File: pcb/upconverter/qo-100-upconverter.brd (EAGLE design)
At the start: 90 x 57 mm, 172 parts, among them CON1 3P-SH-SIDE, CON2 2EDG-2P-5MM, U1 EFM32TG11B120F128GM32, U10 MIC23155, U11 LT8636, U12 MCP3421-A0, U13 MCP6C02-020, U14 ADP7142AUJZ-3.3, U15 ADP7142AUJZ-3.3, U16 ADP3334, U17 ADM7171ACPZ-5.0, U2 DSB321SDA, U3 ADF4351, U4 F1951NBGI, U5 MAX2671, U6 2450BP15E0100, U7 F1478NLGA, U8 F1951NBGI, U9 ADL5606

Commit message: Upconverter assembly BOM changes
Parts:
- C25: value 100nF -> 150pF
- C27: value 100nF -> 150pF + 18 nH
- R4, R5: value 0 Ohms -> 100 Ohms
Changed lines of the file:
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@@
 <drawing>
 <settings>
-<setting alwaysvectorfont="yes"/>
+<setting alwaysvectorfont="no"/>
 <setting verticaltext="up"/>
 </settings>
@@
 </autorouter>
 <elements>
-<element name="C25" library="Capacitor" package="CAP0603" value="100nF" x="81.5" y="45.25" smashed="yes" rot="R180">
+<element name="C25" library="Capacitor" package="CAP0603" value="150pF" x="81.5" y="45.25" smashed="yes" rot="R180">
 <attribute name="NAME" x="81.2536" y="46.666" size="0.8" layer="25" font="vector" ratio="10" rot="SR0" align="center-left"/>
 <attribute name="VALUE" x="84.4464" y="47.282" size="0.8" layer="27" font="vector" ratio="10" rot="SR180" align="center-left"/>
@@
 <attribute name="VALUE" x="72.38" y="45.655" size="0.8" layer="27" font="vector" ratio="10" align="center-left"/>
 </element>
-<element name="C27" library="Capacitor" package="CAP0603" value="100nF" x="69.5" y="44" smashed="yes" rot="R180">
+<element name="C27" library="Capacitor" package="CAP0603" value="150pF + 18 nH" x="69.5" y="44" smashed="yes" rot="R180">
 <attribute name="NAME" x="67.9536" y="45.416" size="0.8" layer="25" font="vector" ratio="10" rot="SR0" align="center-left"/>
 <attribute name="VALUE" x="72.4464" y="46.032" size="0.8" layer="27" font="vector" ratio="10" rot="SR180" align="center-left"/>
@@
 <attribute name="VALUE" x="89.905" y="30.58" size="0.8" layer="27" font="vector" ratio="10" rot="R180" align="center-left"/>
 </element>
-<element name="R4" library="Resistor" package="RES0603" value="0 Ohms" x="81.5" y="24.1" smashed="yes" rot="R180">
+<element name="R4" library="Resistor" package="RES0603" value="100 Ohms" x="81.5" y="24.1" smashed="yes" rot="R180">
 <attribute name="NAME" x="78.4456" y="24.116" size="0.8" layer="25" font="vector" ratio="10" rot="SR0" align="center-left"/>
 <attribute name="TOLERANCE" value="" x="81.5" y="20.8" size="0.8" layer="27" font="vector" ratio="10" rot="R180" display="off"/>
 <attribute name="VALUE" x="84.9544" y="26.132" size="0.8" layer="27" font="vector" ratio="10" rot="SR180" align="center-left"/>
 </element>
-<element name="R5" library="Resistor" package="RES0603" value="0 Ohms" x="81.5" y="25.9" smashed="yes" rot="R180">
+<element name="R5" library="Resistor" package="RES0603" value="100 Ohms" x="81.5" y="25.9" smashed="yes" rot="R180">
 <attribute name="NAME" x="78.4456" y="25.916" size="0.8" layer="25" font="vector" ratio="10" rot="SR0" align="center-left"/>
 <attribute name="TOLERANCE" value="" x="81.5" y="22.6" size="0.8" layer="27" font="vector" ratio="10" rot="R180" display="off"/>

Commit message: Tweaking upconverter performance
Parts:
- C22: value 68nF -> 1uF
- C23: value 2.7nF -> 220nF
- C24: value 910pF -> 2.7nF
- R13: value 866 Ohms -> 150 Ohms
- R15: value 6.65K Ohms -> 1K Ohms
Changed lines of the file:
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@@
 <attribute name="VOLTAGE" value="" x="22.16" y="120.13" size="1.778" layer="27" rot="R180" display="off"/>
 </element>
-<element name="C22" library="Capacitor" package="CAP0603" value="68nF" x="71.7" y="27.3" smashed="yes">
+<element name="C22" library="Capacitor" package="CAP0603" value="1uF" x="71.7" y="27.3" smashed="yes">
 <attribute name="NAME" x="68.0536" y="27.416" size="0.8" layer="25" font="vector" ratio="10" rot="SR0" align="center-left"/>
 <attribute name="VALUE" x="68.7536" y="25.268" size="0.8" layer="27" font="vector" ratio="10" rot="SR0" align="center-left"/>
 <attribute name="VOLTAGE" value="" x="117.42" y="-60.33" size="1.778" layer="27" display="off"/>
 </element>
-<element name="C23" library="Capacitor" package="CAP0603" value="2.7nF" x="71.7" y="30.7" smashed="yes">
+<element name="C23" library="Capacitor" package="CAP0603" value="220nF" x="71.7" y="30.7" smashed="yes">
 <attribute name="NAME" x="71.4536" y="32.116" size="0.8" layer="25" font="vector" ratio="10" rot="SR0" align="center-left"/>
 <attribute name="VALUE" x="68.7536" y="28.668" size="0.8" layer="27" font="vector" ratio="10" rot="SR0" align="center-left"/>
 <attribute name="VOLTAGE" value="" x="122.5" y="-56.93" size="1.778" layer="27" display="off"/>
 </element>
-<element name="C24" library="Capacitor" package="CAP0603" value="910pF" x="74.4" y="29.9" smashed="yes" rot="R90">
+<element name="C24" library="Capacitor" package="CAP0603" value="2.7nF" x="74.4" y="29.9" smashed="yes" rot="R90">
 <attribute name="NAME" x="75.784" y="28.3536" size="0.8" layer="25" font="vector" ratio="10" rot="SR90" align="center-left"/>
 <attribute name="VALUE" x="76.432" y="26.9536" size="0.8" layer="27" font="vector" ratio="10" rot="SR90" align="center-left"/>
@@
 <attribute name="VALUE" x="75.1544" y="27.632" size="0.8" layer="27" font="vector" ratio="10" rot="SR180" align="center-left"/>
 </element>
-<element name="R13" library="Resistor" package="RES0603" value="866 Ohms" x="74.4" y="26.5" smashed="yes" rot="R90">
+<element name="R13" library="Resistor" package="RES0603" value="150 Ohms" x="74.4" y="26.5" smashed="yes" rot="R90">
 <attribute name="NAME" x="75.884" y="25.0456" size="0.8" layer="25" font="vector" ratio="10" rot="SR90" align="center-left"/>
 <attribute name="TOLERANCE" value="" x="126.47" y="100.16" size="1.778" layer="27" rot="R90" display="off"/>
 <attribute name="VALUE" x="76.432" y="23.0456" size="0.8" layer="27" font="vector" ratio="10" rot="SR90" align="center-left"/>
 </element>
-<element name="R15" library="Resistor" package="RES0603" value="6.65K Ohms" x="71.7" y="29" smashed="yes" rot="R180">
+<element name="R15" library="Resistor" package="RES0603" value="1K Ohms" x="71.7" y="29" smashed="yes" rot="R180">
 <attribute name="NAME" x="68.0456" y="28.416" size="0.8" layer="25" font="vector" ratio="10" rot="SR0" align="center-left"/>
 <attribute name="TOLERANCE" value="" x="-9.58" y="81.07" size="1.778" layer="27" rot="R180" display="off"/>

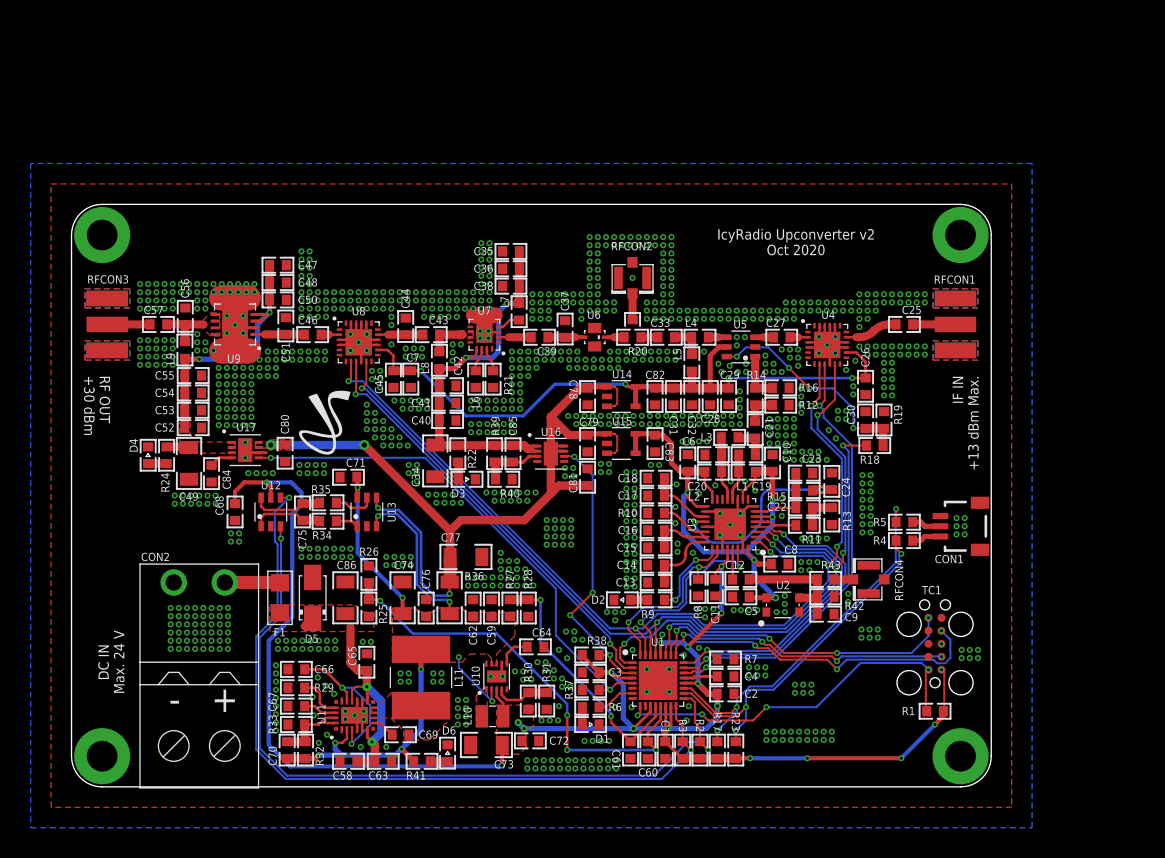
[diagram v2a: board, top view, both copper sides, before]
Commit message: Upconverter v3 sent to production
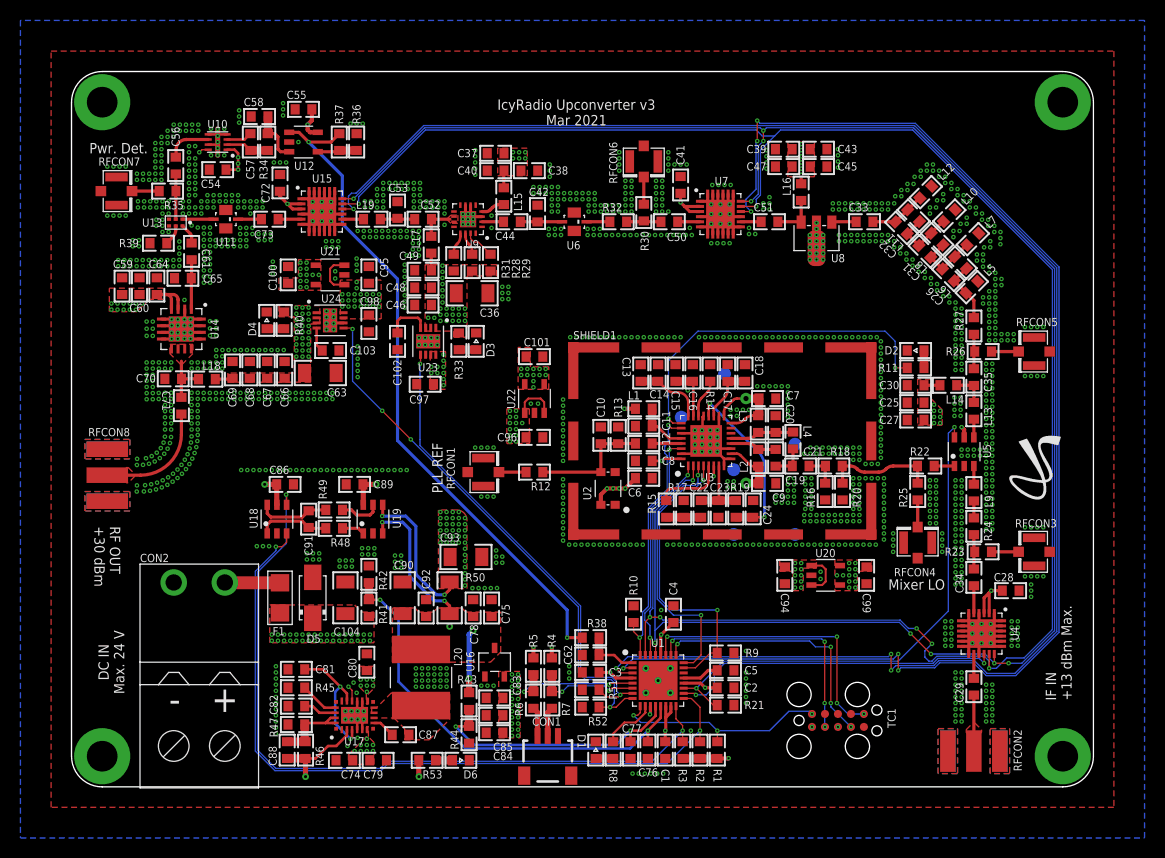
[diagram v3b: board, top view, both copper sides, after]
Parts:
- added C100, C101, C99: 10uF, Capacitor:CAP0603
- added C102, C103: 1nF, Capacitor:CAP0603
- added C104: 10uF, Capacitor:CAP1206
- added C87, C91, C92: 100nF, Capacitor:CAP0603
- added C88: 10pF, Capacitor:CAP0603
- added C89, C94, C95, C96, C97, C98: 1uF, Capacitor:CAP0603
- added C90: 100uF, Capacitor:CAP1206
- added C93: 22uF, Capacitor:CAP1206
- added L12, L13: 3.3nH, Inductor:IND0603
- added L14: 1.8nH, Inductor:IND0603
- added L15: 1.5nH, Inductor:IND0603
- added L16: 470nH, Inductor:IND0603
- added L17: 2.2nH, Inductor:IND0603
- added L18: 62nH, Inductor:IND0603
- added L19: 0 Ohms, Inductor:IND0603
- added L20: 4.7uH, Inductor:IND0606
- added R44: 75K Ohms, Resistor:RES0603
- added R45: 41.2K Ohms, Resistor:RES0603
- added R46: 1M Ohms, Resistor:RES0603
- added R47: 221K Ohms, Resistor:RES0603
- added R48, R49: 10K Ohms, Resistor:RES0603
- added R50: 0.03 Ohms, Resistor:RES1206
- added R51, R52: 100K Ohms, Resistor:RES0603
- added R53: 1K Ohms, Resistor:RES0603
- added RFCON5, RFCON6, RFCON7: RFCON-U.FL, RF Connector:U.FL
- added RFCON8: RFCON-SMA-EDGE, RF Connector:SMA-EDGE
- added SHIELD1: SHIELD-TE-2118728, Shield:2118728
- added TP1, TP2, TP3, TP4, TP5, TP6: TESTPOINT-1.27MM, PADs:PAD1.27MM
- added U18: MCP3421-A0, Microchip:SOT23-6
- added U19: MCP6C02-020, Microchip:SOT23-6
- added U20, U21, U22: ADP7142AUJZ-3.3, Analog Devices:SOT23-5
- added U23, U24: ADM7171ACPZ-5.0, Analog Devices:LFCSP8_3X3
- C10: value 100nF -> 10pF
- C25: value 150pF -> 1uF
- C26: value 100nF -> 1.2pF
- C27: value 150pF + 18 nH -> 100nF
- C28, C4: value 1uF -> 100nF
- C29: value 100nF -> 150pF
- C30: value 100pF -> 47pF
- C31: value 47pF -> 1.8pF
- C32: value 47pF -> 1.5pF
- C33: value 220pF -> 1.5pF
- C34: value 100uF -> 150pF; device Capacitor:CAP1206 -> Capacitor:CAP0603
- C35: value 1uF -> 220pF
- C36: value 1nF -> 100uF; device Capacitor:CAP0603 -> Capacitor:CAP1206
- C37: value 0.5pF -> 1uF
- C38, C55, C7: value 15pF -> 100nF
- C39: value 10pF -> 1uF
- C40: value 1uF -> 33pF
- C41: value 1nF -> 100nF
- C42: value 15pF -> 0.8pF
- C43, C9: value 10pF -> 100nF
- C44: value 1.2pF -> 10pF
- C45: value 100nF -> 47pF
- C46: value 15pF -> 1uF
- C47: value 10uF -> 15pF
- C48: value 10nF -> 100nF
- C49: value 100uF -> 33pF; device Capacitor:CAP1206 -> Capacitor:CAP0603
- C5: value 100nF -> 1uF
- C50: value 100pF -> 15pF
- C51: value 2pF -> 15pF
- C52: value 1uF -> 22pF
- C53: value 10nF -> 0.7pF
- C54: value 100pF -> 4.7uF
- C56: value 3.3pF -> 15pF
- C57: value 15pF -> 10nF
- C58: value 4.7uF -> 1uF
- C59: value 100nF -> 10uF
- C60: value 470pF -> 10nF
- C61: value 470pF -> 15pF
- C62: value 4.7uF -> 10nF
- C63: value 1uF -> 100uF; device Capacitor:CAP0603 -> Capacitor:CAP1206
- C64: value 470pF -> 100pF
- C65: value 1uF -> 2pF
- C68: value 100nF -> 100pF
- C69: value 100nF -> 15pF
- C70: value 10pF -> 3.3pF
- C71: value 1uF -> 15pF
- C73: value 100uF -> 15pF; device Capacitor:CAP1206 -> Capacitor:CAP0603
- C74: value 100uF -> 4.7uF; device Capacitor:CAP1206 -> Capacitor:CAP0603
- C76: value 100nF -> 470pF
- C77: value 22uF -> 470pF; device Capacitor:CAP1206 -> Capacitor:CAP0603
- C78: value 1uF -> 4.7uF
- C82: value 10uF -> 10nF
- C83: value 10uF -> 100nF
- C84: value 1nF -> 10uF
- C85: value 470pF -> 10uF
- C86: value 10uF -> 100nF; device Capacitor:CAP1206 -> Capacitor:CAP0603
- L1: value 3.3nH -> 1uH
- L10: value 2.2uH -> 3.9nH; device Inductor:IND2520 -> Inductor:IND0603
- L11: value 4.7uH -> 5.6nH; device Inductor:IND0606 -> Inductor:IND0603
- L2: value 10nH -> 3.3nH
- L3: value 3.3nH -> 10nH
- L5: value 1.8nH -> 4.7nH
- L6: value 3.9nH -> 12nH
- L7: value 3nH -> 3.3nH
- L8: value 62nH -> 3.9nH
- L9: value 62nH -> 18nH
- R10: value 5.1K Ohms -> 100K Ohms
- R11: value DNP -> 330 Ohms
- R12: value 105 Ohms -> 0 Ohms
- R13: value 150 Ohms -> 10K Ohms
- R14: value 61.9 Ohms -> 5.1K Ohms
- R15, R23: value 1K Ohms -> DNP
- R17: value 1K Ohms -> 150 Ohms
- R18: value 100 Ohms -> 61.9 Ohms
- R19: value 100K Ohms -> 1K Ohms
- R20: value 0 Ohms -> 105 Ohms; device Resistor:RES0603-SEL -> Resistor:RES0603
- R22, R24: value 510 Ohms -> 0 Ohms
- R25: value 100K Ohms -> DNP
- R26, R35: value 10K Ohms -> DNP
- R27: value 100K Ohms -> 0 Ohms
- R28: value 75K Ohms -> 1K Ohms
- R29: value 41.2K Ohms -> 0 Ohms
- R30: value 309K Ohms -> DNP
- R31: value 71.5K Ohms -> 1.5K Ohms
- R32: value 1M Ohms -> 0 Ohms
- R33: value 221K Ohms -> 510 Ohms
- R34: value 10K Ohms -> 0 Ohms
- R36: value 0.03 Ohms -> 1K Ohms; device Resistor:RES1206 -> Resistor:RES0603
- R37: value 100K Ohms -> 2K Ohms
- R38, R7: value 100K Ohms -> 100 Ohms
- R39: value 210K Ohms -> 49.9 Ohms
- R4, R5: value 100 Ohms -> 1K Ohms
- R40: value 64.9K Ohms -> 510 Ohms
- R41: value 510 Ohms -> 100K Ohms
- R43: value 0 Ohms -> 100K Ohms
- R6: value 330 Ohms -> 100 Ohms
- R8: value 100K Ohms -> 330 Ohms
- R9: value 330 Ohms -> 100K Ohms
- RFCON1, RFCON3: value RFCON-SMA-EDGE -> RFCON-U.FL; device RF Connector:SMA-EDGE -> RF Connector:U.FL
- RFCON2: value RFCON-U.FL -> RFCON-SMA-EDGE; device RF Connector:U.FL -> RF Connector:SMA-EDGE
- U10: value MIC23155 -> LTC5597; device Microchip:DFN10 -> Analog Devices:DFN8_2X2
- U11: value LT8636 -> 2450BP15E0100; device Analog Devices:QFN20_ASYM_CORNER -> Generic Filter:2450BP15E0100
- U12: value MCP3421-A0 -> MCP6V31; device Microchip:SOT23-6 -> Microchip:SOT23-5
- U13: value MCP6C02-020 -> DC2337J5010AHF; device Microchip:SOT23-6 -> Anaren:DC2337J5010AHF
- U14: value ADP7142AUJZ-3.3 -> ADL5606; device Analog Devices:SOT23-5 -> Analog Devices:LFCSP16_4X4
- U15: value ADP7142AUJZ-3.3 -> F1958NBGK; device Analog Devices:SOT23-5 -> Renesas:QFN24_2
- U16: value ADP3334 -> MCP1700-330; device Analog Devices:LFCSP8_3X3 -> Microchip:SOT23
- U17: value ADM7171ACPZ-5.0 -> LT8636; device Analog Devices:LFCSP8_3X3 -> Analog Devices:QFN20_ASYM_CORNER
- U4: value F1951NBGI -> F1958NBGK; device Renesas:QFN24 -> Renesas:QFN24_2
- U7: value F1478NLGA -> F1958NBGK; device Renesas:QFN16 -> Renesas:QFN24_2
- U8: value F1951NBGI -> ADL5601; device Renesas:QFN24 -> Analog Devices:SOT89
- U9: value ADL5606 -> F1490NLGA; device Analog Devices:LFCSP16_4X4 -> Renesas:QFN16
- moved RFCON3 93.4 mm to (94.2, 23.0), turned to 180 degrees
- moved R24 79.3 mm to (88.3, 25.5), turned to 270 degrees
- moved L9 78.5 mm to (88.3, 28.8), turned to 90 degrees
- moved LOGO1 69.6 mm to (97.0, 34.5)
- moved C60 67.4 mm to (6.65, 49.0), turned to 90 degrees
- moved L10 66.3 mm to (85.9, 55.9), turned to 225 degrees
- moved L11 66.1 mm to (82.4, 55.9), turned to 135 degrees
- moved C61 65.0 mm to (11.8, 52.4)
- moved R26 63.9 mm to (89.2, 42.6), turned to 0 degrees
- moved C58 63.7 mm to (18.4, 65.6)
- moved R32 60.1 mm to (53.5, 55.3), turned to 0 degrees
- moved C72 59.8 mm to (20.4, 59.1), turned to 90 degrees
- moved U10 59.0 mm to (14.3, 63.1), turned to 180 degrees
- moved R37 59.0 mm to (26.2, 63.1), turned to 270 degrees
- moved RFCON2 57.1 mm to (88.3, 3.50), turned to 0 degrees
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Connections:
- removed net !IF_ATT_CS: U1.22, U4.9
- removed net !PA_STG1_BIAS_EN: R38.1, U1.3, U16.6
- removed net !RF_ATT_CS: U1.2, U8.9
- removed net 3V3_ATT_MIXER_CLEAN: C26.1, C28.1, C29.1, C31.1, C32.1, C45.1, C7.1, C82.1, L5.2, U14.4, U14.5, U4.14, U5.5, U8.14
- removed net 3V3_FB: R30.1, R31.2, U10.4
- removed net 3V3_SOFTSTART: C64.1, U10.6
- removed net 3V3_SW: L10.1, U10.1
- removed net 5V0_PA_STG1_CLEAN: C34.1, C35.1, C36.1, C38.1, C40.1, C41.1, C42.1, C85.1, L7.2, L8.2, R22.2, R39.2, U16.1, U16.2, U7.13
- removed net 5V0_PA_STG2_CLEAN: C47.1, C48.1, C49.1, C50.1, C52.1, C53.1, C54.1, C55.1, L9.2, R24.2, U17.1, U17.2, U17.3, U9.3, U9.4
- removed net N$14: C43.1, L8.1, U7.10, U7.11
- removed net N$18: C57.2, RFCON3.SIG
- removed net N$26: C25.2, U4.17
- removed net N$27: C27.2, U5.3
- removed net N$31: C33.2, R20.2
- removed net N$9: C46.1, U8.2
- removed net PA_STG2_BIAS_EN: R37.2, U1.5, U17.5
- removed net RF_ACC_FILT: C37.1, C39.1, U6.2
- removed net RF_ACC_PRE: C43.2, C44.1, U8.17
- new net 3V3_IF_ATT_MIXER_CLEAN: C25.1, C27.1, C28.1, C30.1, C99.1, L14.2, U20.4, U20.5, U4.2, U4.3, U5.5
- new net 3V3_RF_ATT_PDET_CLEAN: C100.1, C41.1, C54.1, C55.1, C72.1, U10.1, U10.8, U12.5, U15.2, U15.3, U21.4, U21.5, U7.2, U7.3
- new net 5V0_PA_STG1_2_CLEAN: C36.1, C37.1, C38.1, C39.1, C40.1, C43.1, C45.1, C46.1, C47.1, C48.1, C49.1, L15.2, L16.2, L17.2, R28.2, R29.2, R31.2, R33.2, U23.1, U23.2, U23.3
- new net 5V0_PA_STG3_CLEAN: C59.1, C60.1, C63.1, C64.1, C66.1, C67.1, C68.1, C69.1, L18.2, R40.2, U14.3, U14.4, U24.1, U24.2, U24.3
- new net IF_ATT_ACC: L9.1, R24.1
- new net IF_ATT_ACC_PROBE: C34.2, R23.1, R24.2
- new net IF_ATT_DCC: C34.1, U4.5
- new net IF_ATT_LE: U1.18, U4.16
- new net IF_IN_ACC: C29.2, U4.14
- new net MIXER_IN_DCC: L9.2, U5.3
- new net MIXER_OUT_ACC_PROBE: C35.2, R26.1, R27.2
- new net MIXER_OUT_DCC: L13.1, U5.4
- new net N$24: R23.2, RFCON3.P$3
- new net N$33: C31.2, C32.1, L10.2, L11.1, L8.2
- new net N$34: C32.2, C33.1, L11.2, L12.2
- new net N$35: R30.2, RFCON6.P$3
- new net N$39: L19.2, U15.14
- new net N$42: R39.2, U13.5
- new net N$43: C56.1, U10.6
- new net N$44: C57.2, U10.3
- new net N$45: R22.2, U5.1
- new net N$47: R25.1, RFCON4.P$3
- new net N$48: R35.2, RFCON7.P$3
- new net PA_STG1_2_BIAS_EN: R51.2, U1.7, U23.5
- new net PA_STG3_BIAS_EN: R52.2, U1.8, U24.5
- new net RF_ATT1_LE: U1.2, U7.16
- new net RF_ATT2_LE: U1.3, U15.16
- new net RF_FINAL_ACC: C71.2, RFCON8.SIG
- new net RF_FINAL_DCC: C70.1, C71.1, L18.1, U14.10, U14.11, U14.12, U14.9
- new net RF_LOL_FLT_ACC: C33.2, U8.1
- new net RF_PRE1_ACC: C51.2, U7.14
- new net RF_PRE1_ATT_ACC: R32.1, U6.4
- new net RF_PRE1_ATT_ACC_PROBE: C50.2, R30.1, R32.2
- new net RF_PRE1_ATT_DCC: C50.1, U7.5
- new net RF_PRE1_ATT_FLT_ACC: C42.1, C44.1, U6.2
- new net RF_PRE1_DCC: C51.1, L16.1, U8.3
- new net RF_PRE2_ACC: C52.2, C53.1, L19.1
- new net RF_PRE2_ATT_ACC: C73.2, U11.4
- new net RF_PRE2_ATT_DCC: C73.1, U15.5
- new net RF_PRE2_ATT_FLT_ACC: U11.2, U13.1
- new net RF_PRE2_ATT_FLT_CPL_ACC: C56.2, R35.1, U13.2
- new net RF_PRE2_ATT_FLT_THRU_ACC: C61.1, U13.6
- new net RF_PRE2_DCC: C52.1, L17.1, U9.10, U9.11
- new net VPDET_AMP: R37.1, R38.2, U12.1
- new net VPDET_FLT: C58.1, R34.1, U12.3
- new net VPDET_RAW: C57.1, R34.2, U10.2
- new net VPDET_SENSE: C62.1, R38.1, U1.1
- net !MIXER_SHDN: now also R21.2, U1.19, U5.6; no longer R18.2, U1.23
- net !PLL_MUTE: now also R10.2; no longer R8.2
- net 3V3: now also C4.1, C83.1, C84.1, C85.1, C86.1, R4.2, R5.2, U16.2, U18.5; no longer C11.1, C68.1, C72.1, C73.1, L10.2, R17.2, R23.2, R30.2, R38.2, U10.3, U12.5, U3.28
- net 3V3_PLL_CLEAN: now also C101.1, C7.1, C9.1, L1.2, L2.1, L3.2, U22.4, U22.5; no longer C10.1, C5.1, C83.1, L1.1, L2.2, U15.4, U15.5
- net 5V0: now also C75.1, C78.1, C88.1, C89.1, C90.1, C92.1, L20.2, R43.2, R46.2, R50.2, R53.2, U16.3, U17.2, U19.3, U19.6; no longer C59.1, C62.1, C70.1, C71.1, C74.1, C76.1, L11.2, R27.2, R32.2, R36.2, R41.2, U10.2, U10.8, U10.9, U11.2, U13.3, U13.6
- net 5V0_BST: now also C87.2, U17.7; no longer C69.2, U11.7
- net 5V0_FB: now also C88.2, R46.1, R47.2, U17.19, U17.20; no longer C70.2, R32.1, R33.2, U11.19, U11.20
- net 5V0_INTVCC: now also C81.1, U17.15, U17.3; no longer C66.1, U11.15, U11.3
- net 5V0_ISENSE: now also C93.1, C94.1, C95.1, C96.1, C97.1, C98.1, R50.1, U19.4, U20.1, U20.3, U21.1, U21.3, U22.1, U22.3, U23.7, U23.8, U24.7, U24.8; no longer C77.1, C78.1, C79.1, C80.1, C81.1, R36.1, U13.4, U14.1, U14.3, U15.1, U15.3, U16.7, U16.8, U16.9, U17.7, U17.8
- net 5V0_ISENSE_VN: now also C91.2, R49.1, U18.6; no longer C75.2, R35.1, U12.6
- net 5V0_ISENSE_VP: now also C91.1, R48.1, U18.1; no longer C75.1, R34.1, U12.1
- net 5V0_RT: now also R45.2, U17.17; no longer R29.2, U11.17
- net 5V0_SS: now also C82.1, U17.18; no longer C67.1, U11.18
- net 5V0_SW: now also C87.1, L20.1, U17.10, U17.8, U17.9; no longer C69.1, L11.1, U11.10, U11.8, U11.9
- net 5V0_VSENSE: now also C77.1, R43.1, R44.2; no longer C61.1, R27.1, R28.2
- net GND: now also C100.2, C101.2, C102.2, C103.2, C104.2, C25.2, C27.2, C39.2, C43.2, C46.2, C69.2, C70.2, C75.2, C85.2, C89.2, C90.2, C92.2, C93.2, C94.2, C95.2, C96.2, C97.2, C98.2, C99.2, L10.1, L12.1, L5.1, L7.1, R14.1, R17.1, R20.1, R36.1, R39.1, R44.1, R45.1, R47.1, R49.2, R51.1, R52.1, R9.1, RFCON1.P$1, RFCON1.P$2, RFCON2.GND@0, RFCON2.GND@1, RFCON2.GND@2, RFCON2.GND@3, RFCON3.P$1, RFCON3.P$2, RFCON5.P$1, RFCON5.P$2, RFCON6.P$1, RFCON6.P$2, RFCON7.P$1, RFCON7.P$2, RFCON8.GND@0, RFCON8.GND@1, RFCON8.GND@2, RFCON8.GND@3, SHIELD1.1, SHIELD1.10, SHIELD1.11, SHIELD1.12, SHIELD1.13, SHIELD1.14, SHIELD1.15, SHIELD1.16, SHIELD1.2, SHIELD1.3, SHIELD1.4, SHIELD1.5, SHIELD1.6, SHIELD1.7, SHIELD1.8, SHIELD1.9, TP1.TP, TP2.TP, TP3.TP, TP4.TP, TP5.TP, TP6.TP, U10.4, U10.5, U10.9, U11.1, U11.3, U13.3, U13.4, U14.13, U14.14, U14.15, U14.16, U14.17, U14.5, U14.6, U14.7, U14.8, U15.1, U15.10, U15.11, U15.12, U15.13, U15.15, U15.19, U15.20, U15.21, U15.22, U15.23, U15.24, U15.25, U15.4, U15.6, U15.7, U15.8, U15.9, U16.1, U17.12, U17.13, U17.21, U17.4, U17.5, U17.M1, U17.M2, U17.M3, U17.M4, U18.2, U19.2, U19.5, U20.2, U21.2, U22.2, U23.6, U23.9, U24.6, U24.9, U4.11, U4.7, U4.8, U4.9, U7.10, U7.11, U7.13, U7.15, U7.19, U7.20, U7.21, U7.22, U7.23, U7.24, U7.25, U7.4, U8.2, U9.1, U9.12, U9.3, U9.9; no longer C26.2, C29.2, C31.2, C32.2, C34.2, C35.2, C44.2, C50.2, C51.2, C52.2, C56.2, C61.2, C71.2, C73.2, L6.1, R12.1, R19.1, R26.1, R28.1, R29.1, R31.1, R33.1, R35.2, R37.1, R40.1, R7.1, R8.1, RFCON1.GND@0, RFCON1.GND@1, RFCON1.GND@2, RFCON1.GND@3, RFCON2.P$1, RFCON2.P$2, RFCON3.GND@0, RFCON3.GND@1, RFCON3.GND@2, RFCON3.GND@3, U10.10, U10.11, U11.12, U11.13, U11.21, U11.4, U11.5, U11.M1, U11.M2, U11.M3, U11.M4, U13.2, U13.5, U15.2, U16.5, U17.6, U17.9, U4.16, U4.18, U4.3, U7.17, U7.3, U7.5, U8.1, U8.10, U8.12, U8.13, U8.15, U8.16, U8.18, U8.19, U8.20, U8.21, U8.22, U8.23, U8.24, U8.25, U8.3, U8.6, U9.13, U9.14, U9.15, U9.16, U9.2
- net I2C0_SCL: now also R4.1, R7.2, U1.6; no longer R17.1, R5.2, U1.19
- net I2C0_SDA: now also R5.1, R6.2, U1.5; no longer R23.1, R4.2, U1.18
- net I2C1_SCL: now also U18.3; no longer U12.3
- net I2C1_SDA: now also U18.4; no longer U12.4
- net IF_IN_DCC: now also C29.1, RFCON2.SIG; no longer C25.1, RFCON1.SIG
- net LED: now also R8.2, U1.10; no longer R6.2, U1.7
- net MIXER_LO: now also R18.1, R20.2, R22.1, R25.2; no longer R14.1, R16.2, U5.1
- net N$1: now also L4.2; no longer L3.1
- net N$10: now also R48.2, U19.1; no longer R34.2, U13.1
- net N$11: now also R7.1; no longer R5.1
- net N$12: now also L15.1, U9.4; no longer L7.1, U7.4
- net N$13: now also R11.1; no longer R9.1
- net N$149: now also R53.1; no longer R41.1
- net N$15: now also R28.1, U9.14; no longer R21.2, U7.15
- net N$16: now also R31.1, U9.13; no longer L6.2, U7.14
- net N$17: now also R6.1; no longer R4.1
- net N$2: now also C103.1, U24.4; no longer C84.1, U17.4
- net N$20: now also C102.1, U23.4; no longer C85.2, R39.1, R40.2, U16.3
- net N$21: now also R12.2, RFCON1.P$3; no longer R43.2, RFCON4.P$3
- net N$22: now also C5.1; no longer C4.1
- net N$23: now also R33.1; no longer R22.1
- net N$25: now also R8.1; no longer R6.1
- net N$28: now also R26.2, RFCON5.P$3; no longer C27.1, U4.2
- net N$29: now also R16.2, R18.2; no longer R12.2, R14.2
- net N$3: now also R40.1; no longer R24.1
- net N$30: now also C44.2, U9.2; no longer C39.2, U7.2
- net N$32: now also C26.2, C31.1, L6.2, L7.2, L8.1; no longer R20.COM, RFCON2.P$3
- net N$4: now also R29.1, U9.15; no longer C30.1, R18.1, R19.2, U5.6
- net N$5: now also C61.2, C65.1, U14.1; no longer C46.2, C51.1, U9.1
- net N$6: now also C35.1, L13.2, L14.1; no longer C33.1, L4.2, L5.1
- net N$67: now also L3.1, L4.1; no longer L2.1, L3.2
- net N$69: now also L2.2; no longer L1.2
- net N$7: now also R36.2, R37.2, U12.4; no longer L4.1, U5.4
- net N$8: now also C11.1, L1.1, U3.28; no longer C56.1, C57.1, L9.1, U9.10, U9.11, U9.12, U9.9
- net N$84: now also R15.1, R17.2; no longer R11.1, R13.2
- net N$88: now also R14.2; no longer R10.2
- net PLL_CP_VOUT: now also R19.2; no longer R15.2
- net PLL_EN: now also R9.2, U1.23; no longer R7.2, U1.24
- net PLL_FASTLOCK_SW: now also R15.2; no longer R11.2
- net PLL_LE: now also U1.24; no longer U1.1
- net PLL_LOCK: now also R11.2; no longer R9.2
- net PLL_REF_DCC: now also C10.1, R12.1, R13.2; no longer C9.1, R42.2, R43.1
- net PLL_VTUNE: now also R19.1; no longer R15.1
- net RF_ACC: now also C26.1, L5.2, L6.1, R27.1; no longer R20.1, U6.4
- net SPI_MOSI: now also U15.18, U4.18, U7.18; no longer U4.11, U8.11
- net SPI_SCK: now also U15.17, U4.17, U7.17; no longer U4.8, U8.8
- net VIN: now also C104.1, C74.1, C79.1, C80.1, R41.2, U17.11, U17.14, U17.6; no longer C58.1, C63.1, C65.1, C86.1, R25.2, U11.11, U11.14, U11.6
- net VIN_VSENSE: now also C76.1, R41.1, R42.2; no longer C60.1, R25.1, R26.2
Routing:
- net RF_ATT2_LE: track 0.00 -> 165.8 mm, vias 0 -> 4
- net RF_ATT1_LE: track 0.00 -> 130.1 mm, vias 0 -> 6
- net 3V3: track 167.3 -> 59.4 mm, vias 18 -> 32
- net SPI_SCK: track 96.5 -> 190.6 mm, vias 6 -> 8
- net SPI_MOSI: track 98.3 -> 186.2 mm, vias 6 -> 10
- net 3V3_ATT_MIXER_CLEAN: track 66.2 -> 0.00 mm, vias 4 -> 0
- net VPDET_AMP: track 0.00 -> 66.1 mm, vias 0 -> 2
- net GND: track 90.9 -> 152.2 mm, vias 1120 -> 1519
- net 5V0_ISENSE: track 87.5 -> 27.5 mm, vias 4 -> 94
- net PA_STG3_BIAS_EN: track 0.00 -> 53.8 mm, vias 0 -> 4
- net PA_STG2_BIAS_EN: track 50.0 -> 0.00 mm, vias 2 -> 0
- net PA_STG1_2_BIAS_EN: track 0.00 -> 46.6 mm, vias 0 -> 2
- net !IF_ATT_CS: track 43.1 -> 0.00 mm, vias 2 -> 0
- net !RF_ATT_CS: track 42.3 -> 0.00 mm, vias 2 -> 0
- net 5V0_PA_STG1_CLEAN: track 38.2 -> 0.00 mm, vias 2 -> 0
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- added copper zone on layer 15, net 3V3
- added copper zone on layer 1, net 3V3_IF_ATT_MIXER_CLEAN
- added copper zone on layer 15, net 3V3_IF_ATT_MIXER_CLEAN
- added copper zone on layer 1, net 3V3_PLL_CLEAN
- added copper zone on layer 15, net 3V3_PLL_CLEAN
- added copper zone on layer 1, net 3V3_RF_ATT_PDET_CLEAN
- added copper zone on layer 15, net 3V3_RF_ATT_PDET_CLEAN
- added copper zone on layer 15, net 5V0_ISENSE
- added copper zone on layer 1, net 5V0_PA_STG1_2_CLEAN
- added copper zone on layer 15, net 5V0_PA_STG1_2_CLEAN
- added copper zone on layer 1, net 5V0_PA_STG3_CLEAN
- added copper zone on layer 15, net 5V0_PA_STG3_CLEAN
- added copper zone on layer 15, net GND
- added copper zone on layer 2, net GND
- added copper zone on layer 1, net IF_IN_DCC
- added copper zone on layer 1, net RF_FINAL_ACC
- added copper zone on layer 1, net RF_FINAL_DCC
- added copper zone on layer 1, net RF_PRE2_DCC
- added copper zone on layer 15, net VIN
- removed copper zone on layer 1, net 3V3_SW
- removed copper zone on layer 1, net 5V0_PA_STG2_CLEAN
- removed copper zone on layer 1, net N$14
- removed copper zone on layer 1, net N$8
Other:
- board size 90 x 57 mm -> 100 x 70 mm
- board text added: "IcyRadio Upconverter v3 Mar 2021"
- board text added: "Mixer LO"
- board text added: "PLL REF"
- board text added: "Pwr. Det."
- board text removed: "IcyRadio Upconverter v2 Oct 2020"

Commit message: Update I2C slave resistors to minimize load effect when powered down
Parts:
- R4, R5: value 1K Ohms -> 47K Ohms
- R6, R7: value 100 Ohms -> 1K Ohms
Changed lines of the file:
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@@
 <attribute name="VALUE" x="51.68" y="0.095" size="0.8" layer="27" font="vector" ratio="10" rot="R90" align="center-left"/>
 </element>
-<element name="R6" library="Resistor" package="RES0603" value="100 Ohms" x="45.2" y="8.5" smashed="yes" rot="R90">
+<element name="R6" library="Resistor" package="RES0603" value="1K Ohms" x="45.2" y="8.5" smashed="yes" rot="R90">
 <attribute name="NAME" x="43.784" y="6.9456" size="0.8" layer="25" font="vector" ratio="10" rot="SR90" align="center-left"/>
 <attribute name="TOLERANCE" value="" x="41.9" y="8.5" size="0.8" layer="27" font="vector" ratio="10" rot="R90" display="off"/>
 <attribute name="VALUE" x="47.232" y="5.0456" size="0.8" layer="27" font="vector" ratio="10" rot="SR90" align="center-left"/>
 </element>
-<element name="R7" library="Resistor" package="RES0603" value="100 Ohms" x="47" y="8.5" smashed="yes" rot="R90">
+<element name="R7" library="Resistor" package="RES0603" value="1K Ohms" x="47" y="8.5" smashed="yes" rot="R90">
 <attribute name="NAME" x="48.384" y="6.9456" size="0.8" layer="25" font="vector" ratio="10" rot="SR90" align="center-left"/>
 <attribute name="TOLERANCE" value="" x="43.7" y="8.5" size="0.8" layer="27" font="vector" ratio="10" rot="R90" display="off"/>
@@
 <attribute name="NAME" x="56.7" y="14.1" size="0.8" layer="25" font="vector" ratio="10" align="center-left"/>
 </element>
-<element name="R4" library="Resistor" package="RES0603" value="1K Ohms" x="47" y="11.8" smashed="yes" rot="R90">
+<element name="R4" library="Resistor" package="RES0603" value="47K Ohms" x="47" y="11.8" smashed="yes" rot="R90">
 <attribute name="NAME" x="46.984" y="13.6456" size="0.8" layer="25" font="vector" ratio="10" rot="SR90" align="center-left"/>
 <attribute name="TOLERANCE" value="" x="47" y="11.8" size="1.778" layer="27" rot="R90" display="off"/>
 <attribute name="VALUE" x="49.032" y="8.3456" size="0.8" layer="27" font="vector" ratio="10" rot="SR90" align="center-left"/>
 </element>
-<element name="R5" library="Resistor" package="RES0603" value="1K Ohms" x="45.2" y="11.8" smashed="yes" rot="R90">
+<element name="R5" library="Resistor" package="RES0603" value="47K Ohms" x="45.2" y="11.8" smashed="yes" rot="R90">
 <attribute name="NAME" x="45.184" y="13.6456" size="0.8" layer="25" font="vector" ratio="10" rot="SR90" align="center-left"/>
 <attribute name="TOLERANCE" value="" x="45.2" y="11.8" size="1.778" layer="27" rot="R90" display="off"/>

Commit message: Revert I2C resistor chnges because they do not work
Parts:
- R4, R5: value 47K Ohms -> 1K Ohms
- R6, R7: value 1K Ohms -> 100 Ohms
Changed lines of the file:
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@@
 <attribute name="VALUE" x="51.68" y="0.095" size="0.8" layer="27" font="vector" ratio="10" rot="R90" align="center-left"/>
 </element>
-<element name="R6" library="Resistor" package="RES0603" value="1K Ohms" x="45.2" y="8.5" smashed="yes" rot="R90">
+<element name="R6" library="Resistor" package="RES0603" value="100 Ohms" x="45.2" y="8.5" smashed="yes" rot="R90">
 <attribute name="NAME" x="43.784" y="6.9456" size="0.8" layer="25" font="vector" ratio="10" rot="SR90" align="center-left"/>
 <attribute name="TOLERANCE" value="" x="41.9" y="8.5" size="0.8" layer="27" font="vector" ratio="10" rot="R90" display="off"/>
 <attribute name="VALUE" x="47.232" y="5.0456" size="0.8" layer="27" font="vector" ratio="10" rot="SR90" align="center-left"/>
 </element>
-<element name="R7" library="Resistor" package="RES0603" value="1K Ohms" x="47" y="8.5" smashed="yes" rot="R90">
+<element name="R7" library="Resistor" package="RES0603" value="100 Ohms" x="47" y="8.5" smashed="yes" rot="R90">
 <attribute name="NAME" x="48.384" y="6.9456" size="0.8" layer="25" font="vector" ratio="10" rot="SR90" align="center-left"/>
 <attribute name="TOLERANCE" value="" x="43.7" y="8.5" size="0.8" layer="27" font="vector" ratio="10" rot="R90" display="off"/>
@@
 <attribute name="NAME" x="56.7" y="14.1" size="0.8" layer="25" font="vector" ratio="10" align="center-left"/>
 </element>
-<element name="R4" library="Resistor" package="RES0603" value="47K Ohms" x="47" y="11.8" smashed="yes" rot="R90">
+<element name="R4" library="Resistor" package="RES0603" value="1K Ohms" x="47" y="11.8" smashed="yes" rot="R90">
 <attribute name="NAME" x="46.984" y="13.6456" size="0.8" layer="25" font="vector" ratio="10" rot="SR90" align="center-left"/>
 <attribute name="TOLERANCE" value="" x="47" y="11.8" size="1.778" layer="27" rot="R90" display="off"/>
 <attribute name="VALUE" x="49.032" y="8.3456" size="0.8" layer="27" font="vector" ratio="10" rot="SR90" align="center-left"/>
 </element>
-<element name="R5" library="Resistor" package="RES0603" value="47K Ohms" x="45.2" y="11.8" smashed="yes" rot="R90">
+<element name="R5" library="Resistor" package="RES0603" value="1K Ohms" x="45.2" y="11.8" smashed="yes" rot="R90">
 <attribute name="NAME" x="45.184" y="13.6456" size="0.8" layer="25" font="vector" ratio="10" rot="SR90" align="center-left"/>
 <attribute name="TOLERANCE" value="" x="45.2" y="11.8" size="1.778" layer="27" rot="R90" display="off"/>
